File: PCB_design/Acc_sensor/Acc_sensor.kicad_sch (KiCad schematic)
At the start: 28 parts, among them Q1 NMOS, Q2 NMOS, SW1 SW_SPST, U1 ESP32-C3, U2 LIS2DE12, U3 DW01A, U4 TLV75509PDBV, U5 TPS22917LDBV

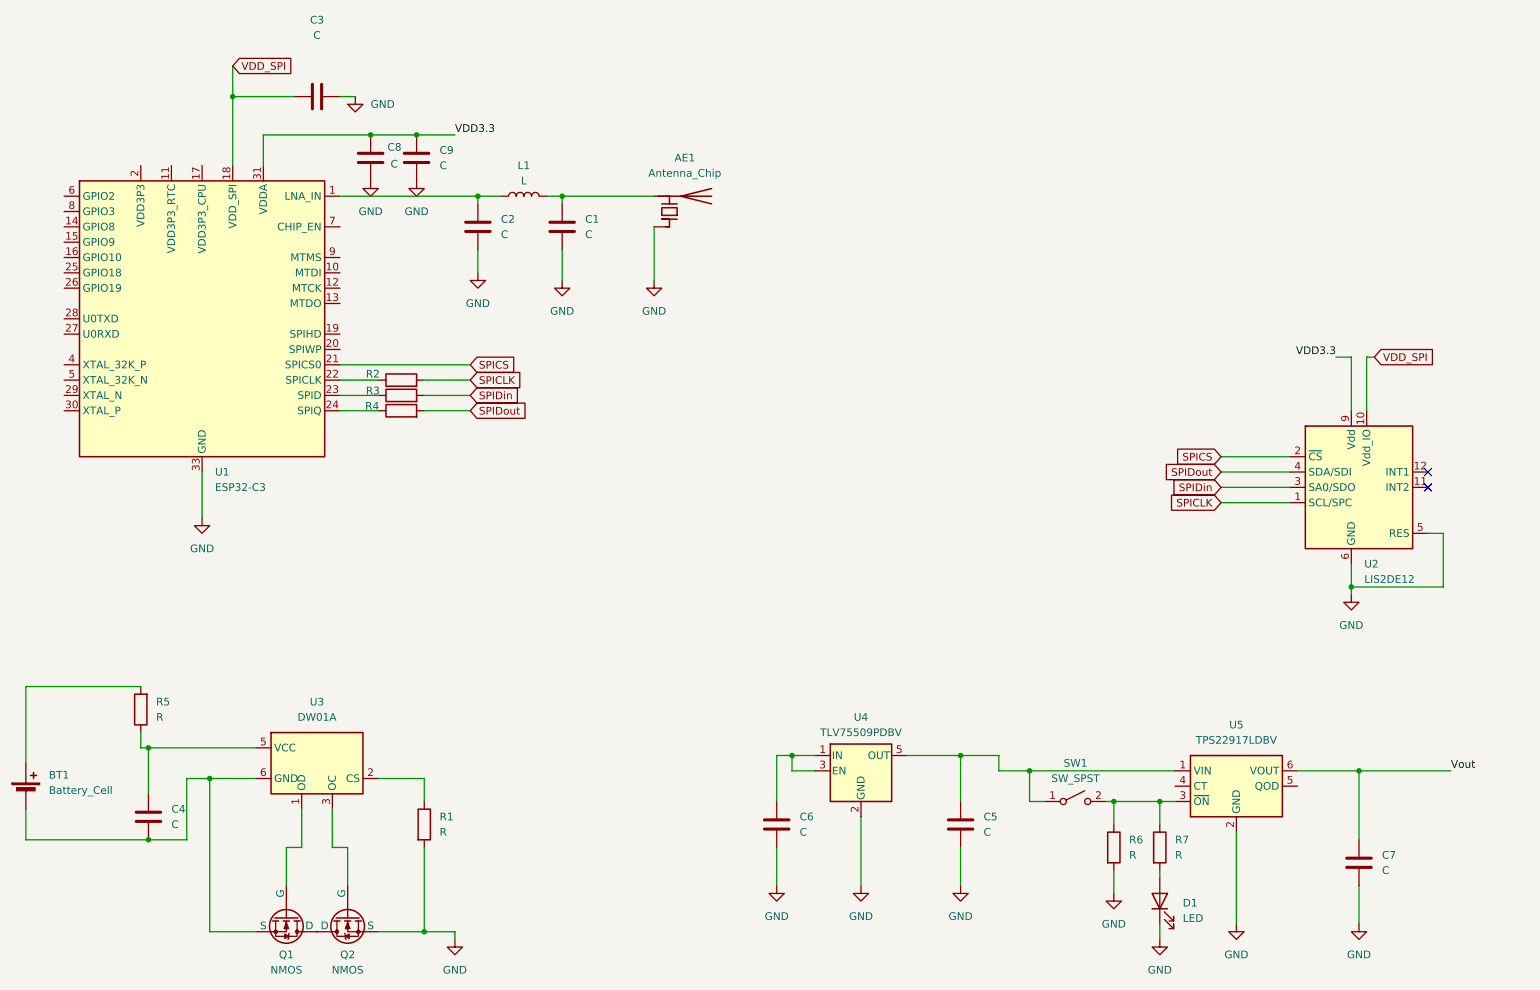
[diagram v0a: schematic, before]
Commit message: upload file
split into acc sensor and BMS file. Yet to copy to have a ppg sensor file
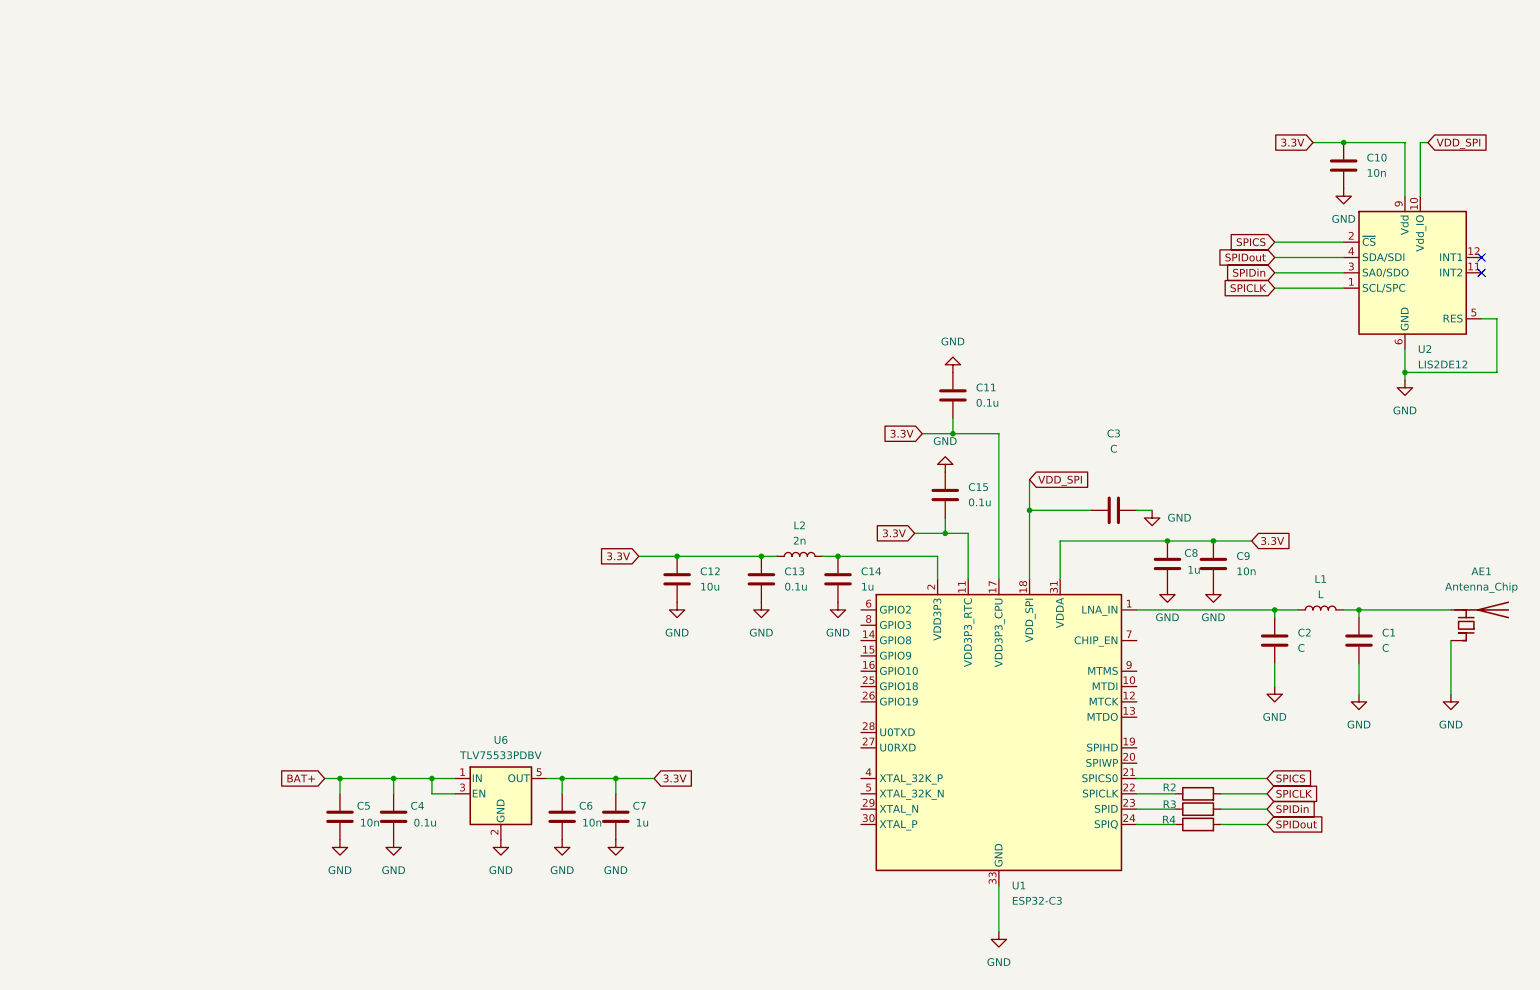
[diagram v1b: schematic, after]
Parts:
- removed BT1: Battery_Cell, symbol Device:Battery_Cell
- removed D1: LED, symbol Device:LED
- removed Q1, Q2: NMOS, symbol Simulation_SPICE:NMOS
- removed R1, R5, R6, R7: R, symbol Device:R
- removed SW1: SW_SPST, symbol Switch:SW_SPST
- removed U3: DW01A, Package_TO_SOT_SMD:SOT-23-6, symbol Battery_Management:DW01A
- removed U4: TLV75509PDBV, Package_TO_SOT_SMD:SOT-23-5, symbol Regulator_Linear:TLV75509PDBV
- removed U5: TPS22917LDBV, Package_TO_SOT_SMD:SOT-23-6, symbol Power_Management:TPS22917LDBV
- added C10: 10n, symbol Device:C
- added C11, C13, C15: 0.1u, symbol Device:C
- added C12: 10u, symbol Device:C
- added C14: 1u, symbol Device:C
- added L2: 2n, symbol Device:L
- added U6: TLV75533PDBV, Package_TO_SOT_SMD:SOT-23-5, symbol Regulator_Linear:TLV75533PDBV
- C4: value C -> 0.1u
- C5, C6, C9: value C -> 10n
- C7, C8: value C -> 1u
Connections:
- net VDD3.3 is gone; now on net 3.3V: C8.1, C9.1, U1.31 (VDDA), U1.32 (VDDA), U2.9 (Vdd)
- net Vout is gone; now on net 3.3V: C7.1
- net GND: now also C4.2, C10.2, C11.1, C12.2, C13.2, C14.2, C15.1, U6.2 (GND)
- net BAT+: now reaches C5.1
- net BAT+: now also C4.1, U6.1 (IN), U6.3 (EN)
- net 3.3V: now reaches C6.1
- net 3.3V: now also U1.11 (VDD3P3_RTC), U1.17 (VDD3P3_CPU), C10.1, C11.2, C12.1, C13.1, C15.2, L2.1, U6.5 (OUT)
- net at U1.2 (VDD3P3), U1.3 (VDD3P3): now also C14.1, L2.2
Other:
- moved on the sheet: AE1, C1, C2, C3, C8, C9, L1, R2, R3, R4, U1, U2

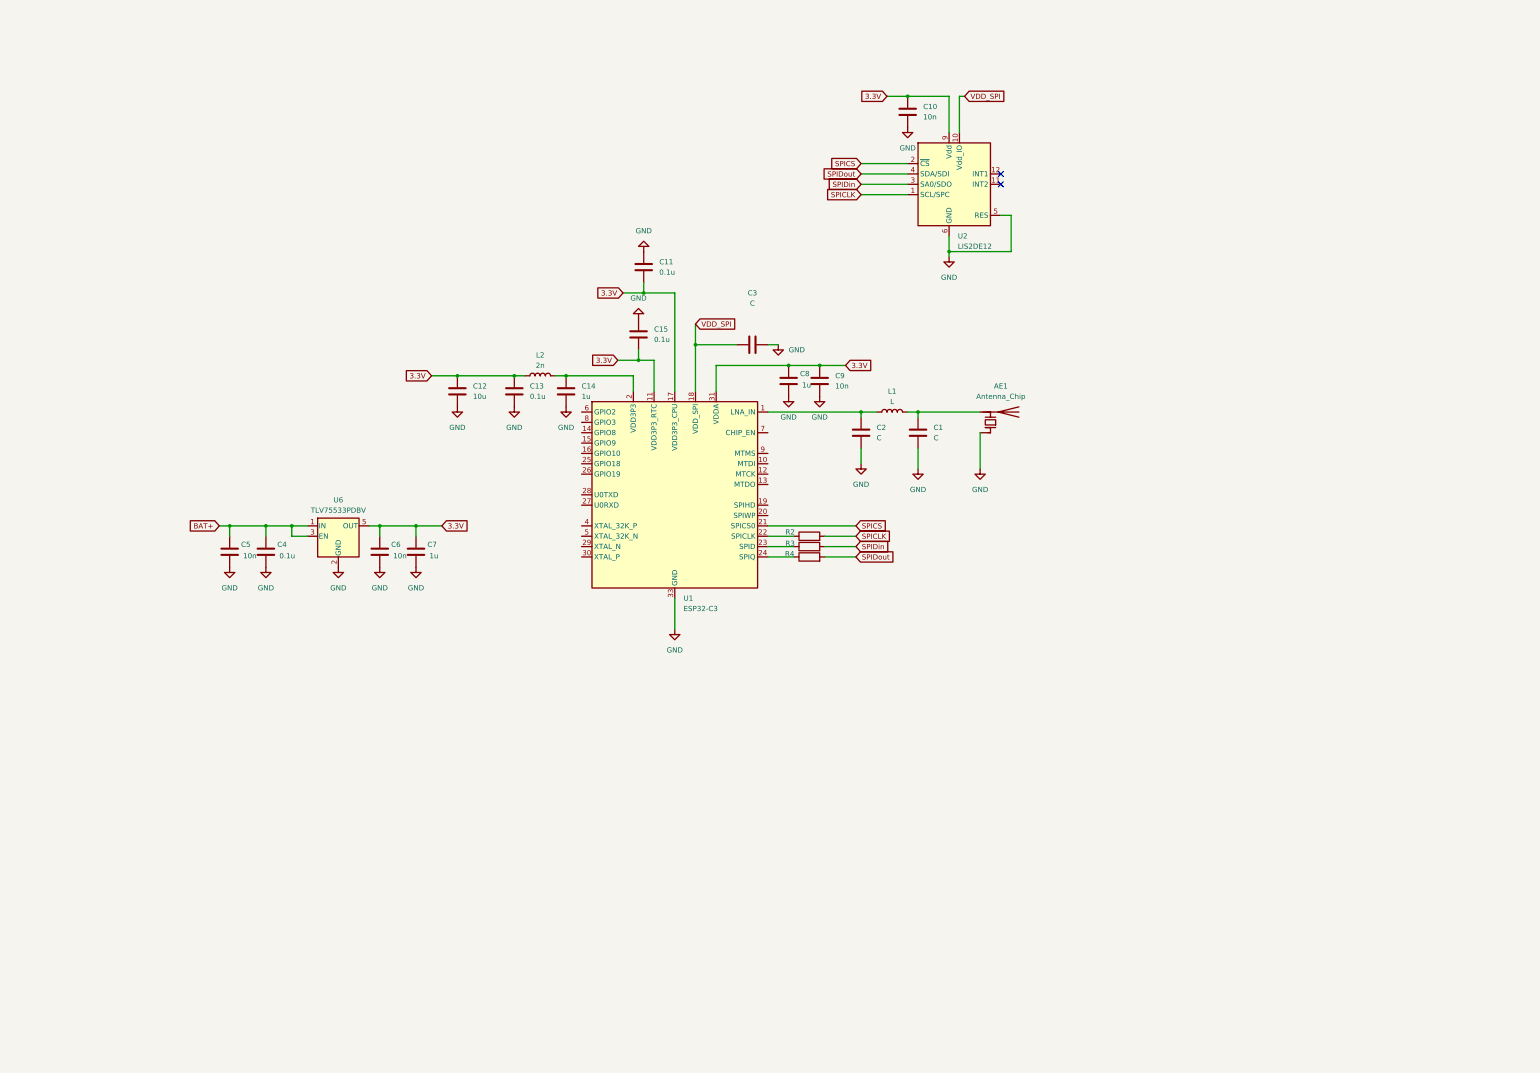
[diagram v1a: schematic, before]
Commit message: integrated BMS back into main schematic
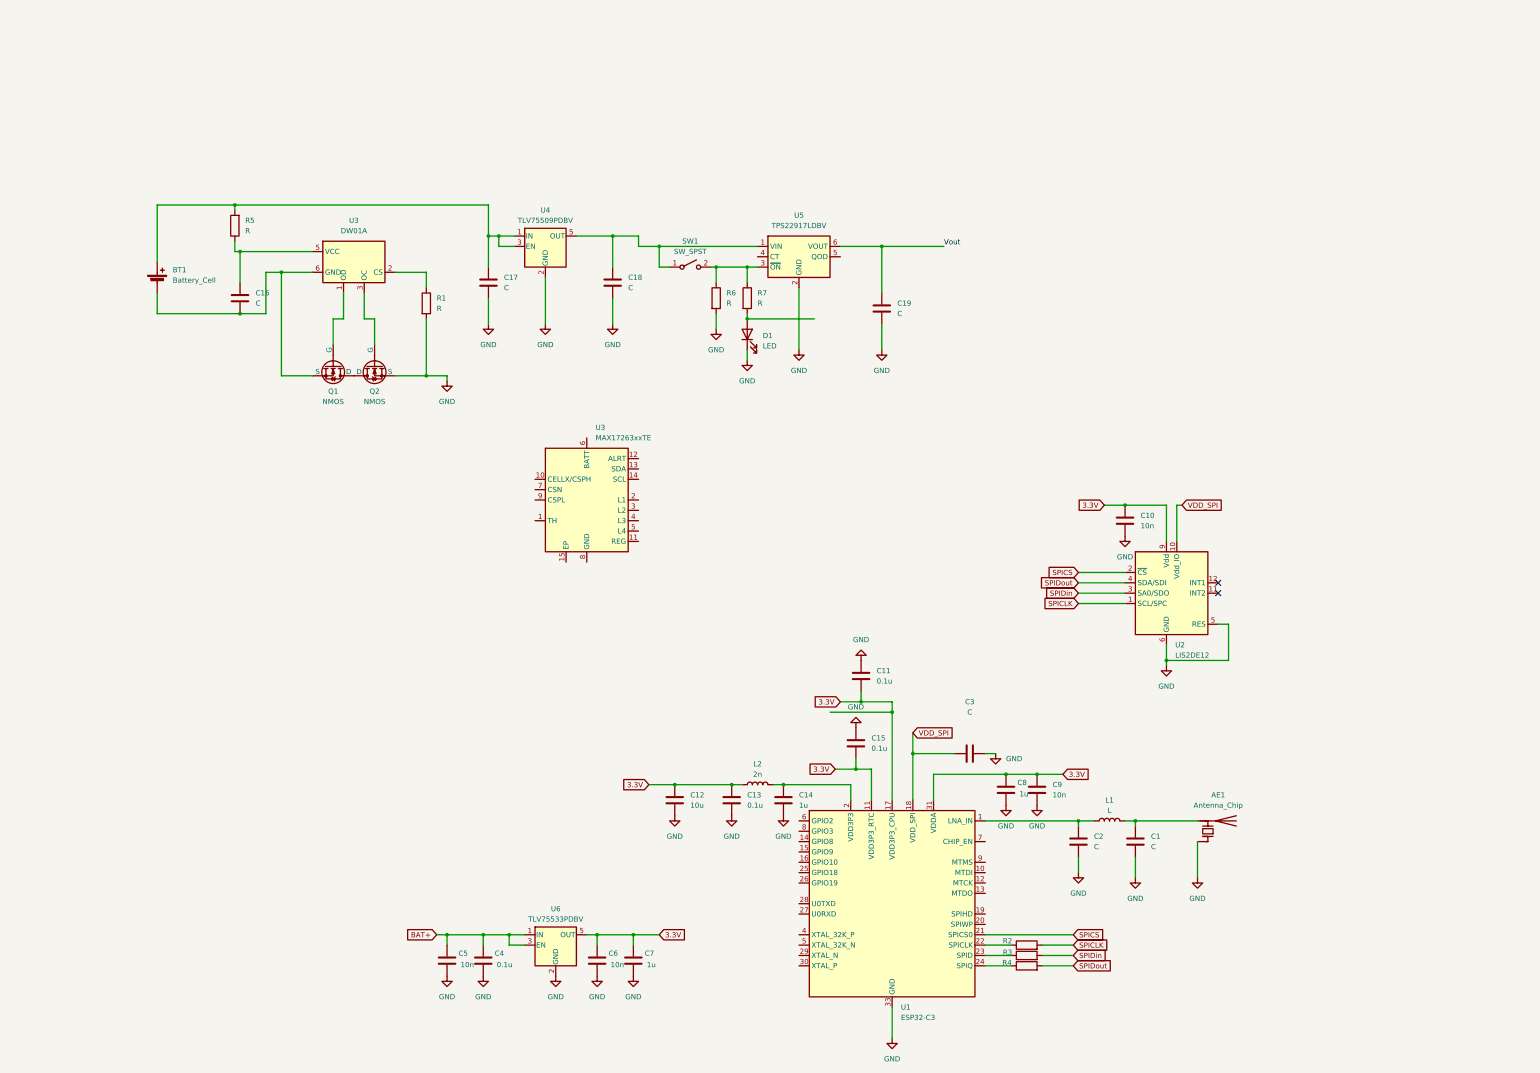
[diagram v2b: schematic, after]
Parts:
- added BT1: Battery_Cell, symbol Device:Battery_Cell
- added C16, C17, C18, C19: C, symbol Device:C
- added D1: LED, symbol Device:LED
- added Q1, Q2: NMOS, symbol Simulation_SPICE:NMOS
- added R1, R5, R6, R7: R, symbol Device:R
- added SW1: SW_SPST, symbol Switch:SW_SPST
- added U3: MAX17263xxTE, Package_DFN_QFN:DFN-14-1EP_3x3mm_P0.4mm_EP1.78x2.35mm, symbol Battery_Management:MAX17263xxTE
- added U3: DW01A, Package_TO_SOT_SMD:SOT-23-6, symbol Battery_Management:DW01A
- added U4: TLV75509PDBV, Package_TO_SOT_SMD:SOT-23-5, symbol Regulator_Linear:TLV75509PDBV
- added U5: TPS22917LDBV, Package_TO_SOT_SMD:SOT-23-6, symbol Power_Management:TPS22917LDBV
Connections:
- net GND: now also C17.2, C18.2, C19.2, D1.1 (K), Q2.3 (S), R1.2, R6.2, U4.2 (GND), U5.2 (GND)
- new net: C18.1, SW1.1 (A), U4.5 (OUT), U5.1 (VIN)
- new net: R6.1, R7.1, SW1.2 (B), U5.3 (~{ON})
- new net: BT1.1 (+), C17.1, R5.2, U4.1 (IN), U4.3 (EN)
- new net: Q1.1 (D), Q2.1 (D)
- new net: Q1.2 (G), U3.1 (OD)
- new net: BT1.2 (-), C16.2, Q1.3 (S), U3.6 (GND)
- new net: Q2.2 (G), U3.3 (OC)
- new net: R1.1, U3.2 (CS)
- new net: C16.1, R5.1, U3.5 (VCC)
- new net: D1.2 (A), R7.2
- new net Vout: C19.1, U5.6 (VOUT)
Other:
- moved on the sheet: AE1, C1, C10, C11, C12, C13, C14, C15, C2, C3, C4, C5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

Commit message: update
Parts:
- removed C4: 0.1u, symbol Device:C
- removed C5, C6: 10n, symbol Device:C
- removed C7: 1u, symbol Device:C
- removed U4: TLV75509PDBV, Package_TO_SOT_SMD:SOT-23-5, symbol Regulator_Linear:TLV75509PDBV
- removed U6: TLV75533PDBV, Package_TO_SOT_SMD:SOT-23-5, symbol Regulator_Linear:TLV75533PDBV
- added U4: MAX30102, OptoDevice:Maxim_OLGA-14_3.3x5.6mm_P0.8mm, symbol Sensor:MAX30102
- added U7: TLV75533PDBV, Package_TO_SOT_SMD:SOT-23-5, symbol Regulator_Linear:TLV75533PDBV
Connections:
- net Vout is gone; now on net 3.3V: C19.1, U5.6 (VOUT)
- net GND: now also U7.2 (GND)
- net at C18.1, SW1.1 (A), U5.1 (VIN): now also U7.5 (OUT)
- net at BT1.1 (+), C17.1, R5.2: now also U7.1 (IN), U7.3 (EN)
- new net: U4.10 (VLED+), U4.9 (VLED+)
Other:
- note added: "Battery Gauge symbol,footprint,model tbc"
- moved on the sheet: AE1, BT1, C1, C10, C11, C12, C13, C14, C15, C16, C19, C2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

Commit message: update
update yesterday group work
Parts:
- C3: value C -> 1u
- R2, R3, R4: value R -> 22
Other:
- note added: "tbc, Ferrite bead may needed."
- note added: "tbc, calculation needed."
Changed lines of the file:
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@@
 		)
 	)
+	(text "tbc, calculation needed."
+		(exclude_from_sim no)
+		(at 163.83 174.752 0)
+		(effects
+			(font
+				(size 1.27 1.27)
+			)
+		)
+	)
+	(text "tbc, Ferrite bead may needed."
+		(exclude_from_sim no)
+		(at 139.954 223.52 0)
+		(effects
+			(font
+				(size 1.27 1.27)
+			)
+		)
+	)
 	(junction
 		(at 137.16 184.15)
@@
 	)
 	(junction
-		(at 91.44 157.48)
-		(diameter 0)
-		(color 0 0 0 0)
-	)
-	(junction
 		(at 76.2 73.66)
 		(diameter 0)
@@
 	(wire
 		(pts
-			(xy 91.44 157.48) (xy 91.44 179.07)
-		)
-		(stroke
-			(width 0)
-			(type default)
-		)
-	)
-	(wire
-		(pts
-			(xy 76.2 157.48) (xy 91.44 157.48)
+			(xy 91.44 154.94) (xy 91.44 179.07)
 		)
 		(stroke
@@
 	(wire
 		(pts
-			(xy 91.44 154.94) (xy 91.44 157.48)
-		)
-		(stroke
-			(width 0)
-			(type default)
-		)
-	)
-	(wire
-		(pts
 			(xy 96.52 167.64) (xy 96.52 179.07)
 		)
@@
 			)
 		)
-		(property "Value" "R"
+		(property "Value" "22"
 			(at 120.396 214.884 90)
 			(effects
@@
 			)
 		)
-		(property "Value" "R"
+		(property "Value" "22"
 			(at 125.476 213.106 0)
 			(effects
@@
 			)
 		)
-		(property "Value" "C"
+		(property "Value" "1u"
 			(at 110.49 157.48 90)
 			(effects
@@
 			)
 		)
-		(property "Value" "R"
+		(property "Value" "22"
 			(at 125.7299 214.63 0)
 			(effects
